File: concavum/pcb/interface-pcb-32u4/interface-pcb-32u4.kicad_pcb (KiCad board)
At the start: 2 copper layers, 30 x 38 mm, 24 parts, among them J1 USB_C_Port, J2 Audio_Jack, J3 ISP_pads, J4 FPC_connector, U1 ATmega32U4-A, U2 MCP23017_SO, Y1 Crystal_16MHz

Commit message: Rename footprints to match KiCad naming scheme
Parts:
- J2: footprint Custom:Audio-Jack-Dual-Side -> Custom:Audio_Jack_Dual_Side
- J3: value ISP_pads -> ISP_Pads; footprint Custom:ISP-Pads -> Custom:ISP_Pads
- J4: footprint Custom:FPC-Connector -> Custom:FPC_Connector
- U1: footprint Custom:TQFP-44-Rounded-Pads -> Custom:TQFP_44_Rounded_Pads
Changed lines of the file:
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@@
     )
   )
-  (footprint "Custom:Audio-Jack-Dual-Side" locked (layer "F.Cu")
+  (footprint "Custom:Audio_Jack_Dual_Side" locked (layer "F.Cu")
     (at 163.6 86.8 -90)
     (property "Sheetfile" "interface-pcb-32u4.kicad_sch")
@@
     )
   )
-  (footprint "Custom:FPC-Connector" (layer "F.Cu")
+  (footprint "Custom:FPC_Connector" (layer "F.Cu")
     (at 154.5 111.6)
     (property "Sheetfile" "interface-pcb-32u4.kicad_sch")
@@
       (net 53 "unconnected-(H1-Pad1)") (pinfunction "1") (pintype "input+no_connect"))
   )
-  (footprint "Custom:TQFP-44-Rounded-Pads" (layer "F.Cu")
+  (footprint "Custom:TQFP_44_Rounded_Pads" (layer "F.Cu")
     (at 153.1 103 -90)
     (descr "44-Lead Plastic Thin Quad Flatpack (PT) - 10x10x1.0 mm Body [TQFP] (see Microchip Packaging Specification 00000049BS.pdf)")
@@
     )
   )
-  (footprint "Custom:ISP-Pads" (layer "F.Cu")
+  (footprint "Custom:ISP_Pads" (layer "F.Cu")
     (at 148.3 93.7 180)
     (property "Sheetfile" "interface-pcb-32u4.kicad_sch")
@@
       (effects (font (size 1.143 1.143) (thickness 0.152)) (justify right))
     )
-    (fp_text value "ISP_pads" (at -3.302 -3.048) (layer "B.Fab") hide
+    (fp_text value "ISP_Pads" (at -3.302 -3.048) (layer "B.Fab") hide
       (effects (font (size 1.143 1.143) (thickness 0.152)) (justify right mirror))
     )

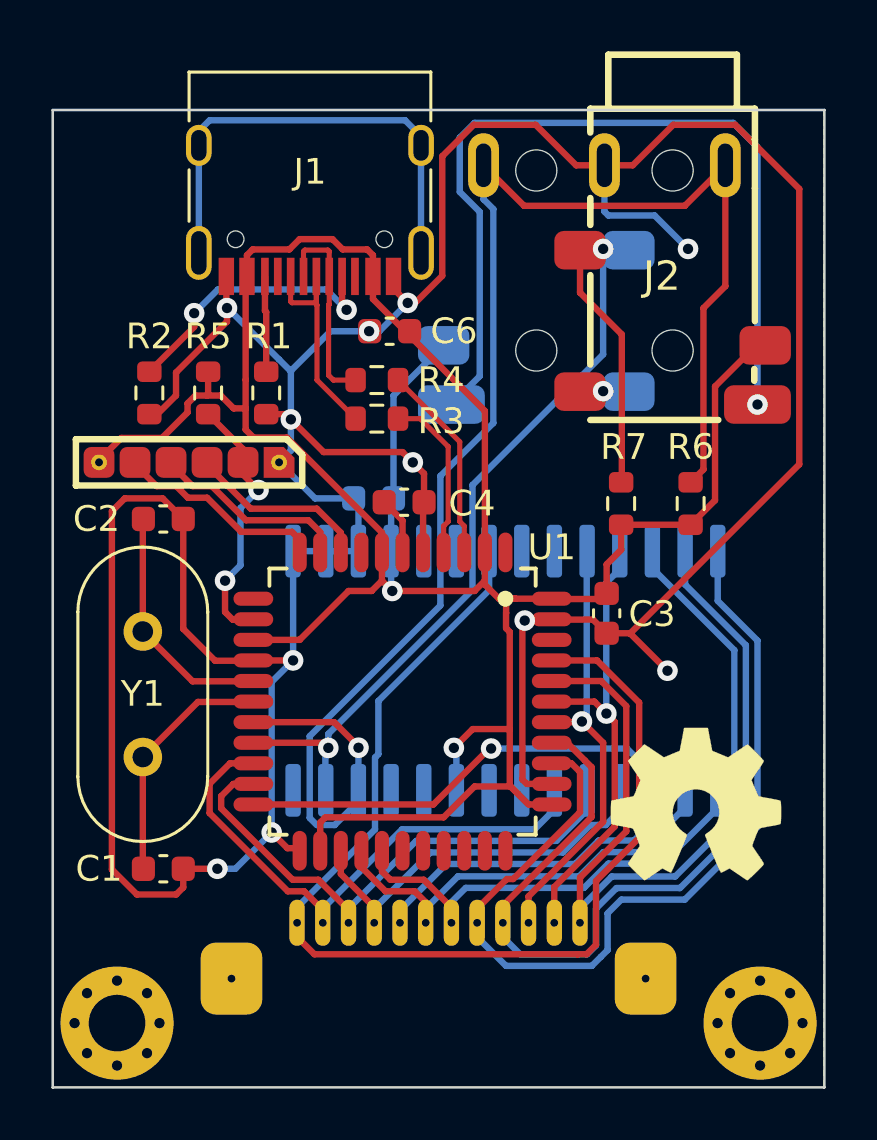
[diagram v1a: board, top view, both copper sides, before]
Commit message: Change FPC connector pinout to increase clearances
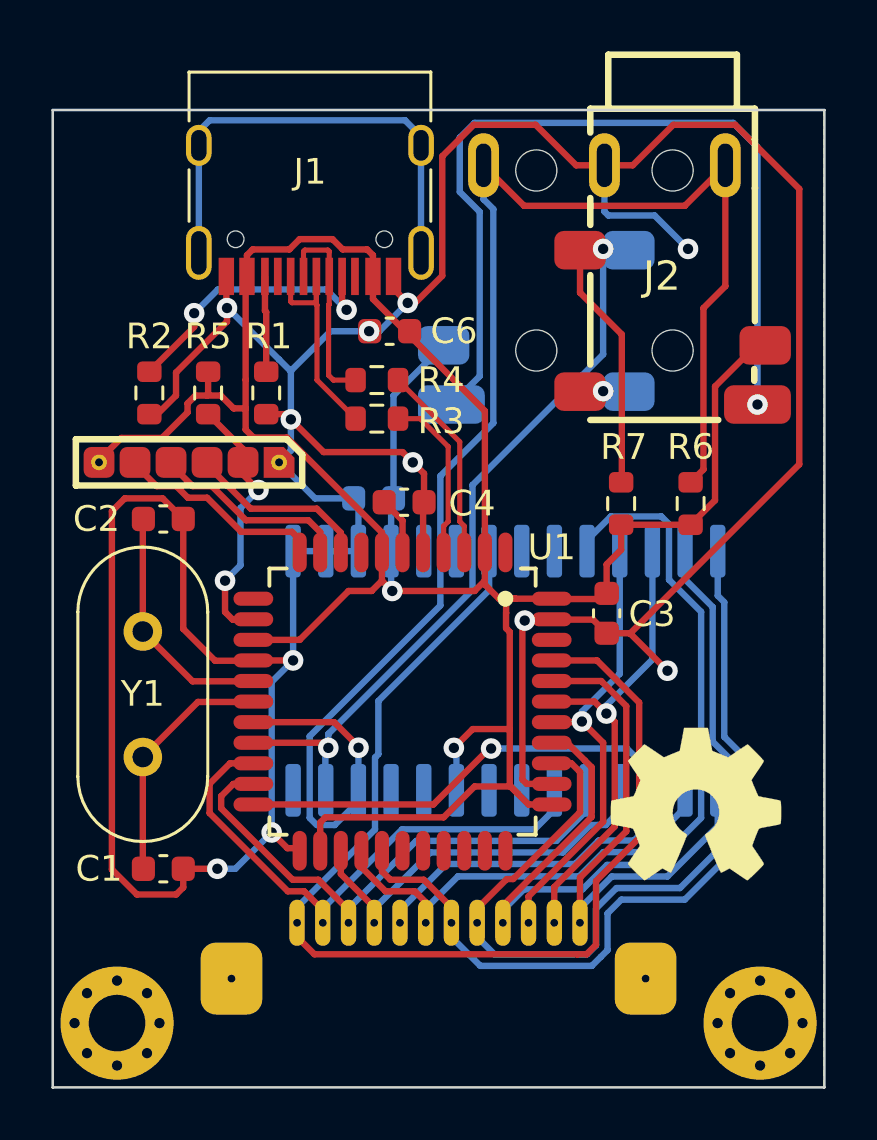
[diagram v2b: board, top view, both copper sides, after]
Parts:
- J4: value FPC_connector -> FPC_Connector
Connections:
- J4 pad 10: /ROW4 -> /ROW5
- J4 pad 11: /ROW5 -> /ROW6
- J4 pad 12: /ROW6 -> /COL6
- J4 pad 7: /COL6 -> /ROW2
- J4 pad 8: /ROW2 -> /ROW3
- J4 pad 9: /ROW3 -> /ROW4
- U1 pad 27: /COL6 -> /ROW2
- U1 pad 36: /ROW2 -> /ROW3
- U1 pad 37: /ROW3 -> /ROW4
- U1 pad 38: /ROW4 -> /ROW5
- U1 pad 39: /ROW5 -> /ROW6
- U1 pad 40: /ROW6 -> /COL6
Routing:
- net /ROW4: track 17.4 -> 35.3 mm, vias 1 -> 0
- net /ROW6: track 32.3 -> 18.7 mm, vias 0 -> 1
- net /ROW2: track 35.9 -> 32.2 mm
- net /COL6: track 18.6 -> 21.2 mm
- net /ROW3: track 34.3 -> 34.9 mm
